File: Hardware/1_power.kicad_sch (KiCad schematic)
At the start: 22 parts

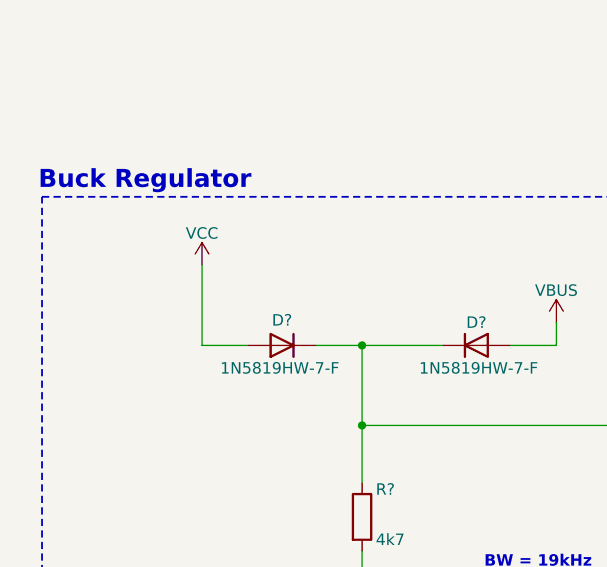
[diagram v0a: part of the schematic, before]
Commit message: feat: Update to use I2C stemma connector
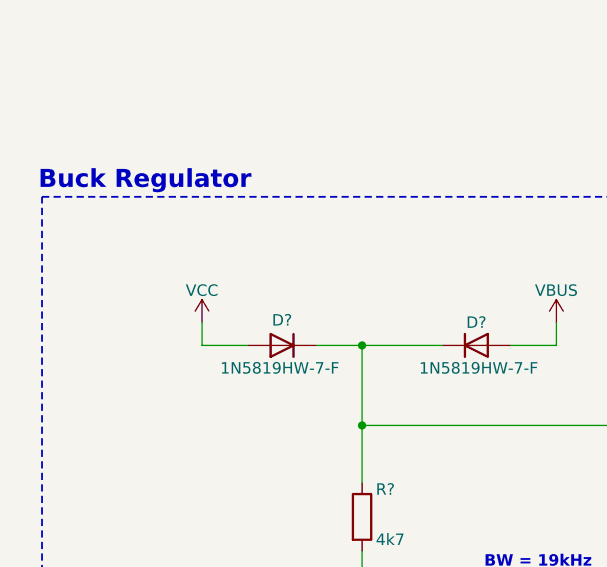
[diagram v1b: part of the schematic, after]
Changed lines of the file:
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@@
 	(wire
 		(pts
-			(xy 41.91 43.18) (xy 41.91 52.07)
+			(xy 41.91 49.53) (xy 41.91 52.07)
 		)
 		(stroke
@@
 	(symbol
 		(lib_id "power:VCC")
-		(at 41.91 43.18 0)
+		(at 41.91 49.53 0)
 		(unit 1)
 		(exclude_from_sim no)
@@
 		(dnp no)
 		(property "Reference" "#PWR025"
-			(at 41.91 46.99 0)
+			(at 41.91 53.34 0)
 			(effects
 				(font
@@
 		)
 		(property "Value" "VCC"
-			(at 41.91 39.624 0)
+			(at 41.91 45.974 0)
 			(effects
 				(font
@@
 		)
 		(property "Footprint" ""
-			(at 41.91 43.18 0)
+			(at 41.91 49.53 0)
 			(effects
 				(font
@@
 		)
 		(property "Datasheet" ""
-			(at 41.91 43.18 0)
+			(at 41.91 49.53 0)
 			(effects
 				(font
@@
 		)
 		(property "Description" "Power symbol creates a global label with name \"VCC\""
-			(at 41.91 43.18 0)
-			(effects
-				(font
+			(at 41.91 49.53 0)
+			(effects
+				(font
